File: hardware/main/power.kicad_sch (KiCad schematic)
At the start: 32 parts, among them Q1 SSM3J338R, Q2 BCP53, Q3 SSM3J338R, Q4 BC817, Q5 SSM3J338R, Q6 BC807, Q7 BC817, Q8 BC817, U5 AP2114H-3.3, U7 LM358

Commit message: WIP: Design of PCB
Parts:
- added R21: 0, Resistor_SMD:R_0603_1608Metric_Pad0.98x0.95mm_HandSolder, symbol Device:R
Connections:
- net +BATT: now also R21.1; no longer JP1.1 (A), Q1.3 (D)
- new net: JP1.1 (A), Q1.3 (D), R21.2
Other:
- note added: "TODO: polarity-proof connectors for the batteries"
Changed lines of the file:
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@@
     (stroke (width 0) (type solid) (color 0 0 0 0))
   )
-  (wire (pts (xy 227.33 49.53) (xy 227.33 46.99))
+  (wire (pts (xy 227.33 46.99) (xy 227.33 55.88))
     (stroke (width 0) (type solid) (color 0 0 0 0))
   )
@@
     (stroke (width 0) (type solid) (color 0 0 0 0))
   )
+  (wire (pts (xy 231.14 55.88) (xy 227.33 55.88))
+    (stroke (width 0) (type solid) (color 0 0 0 0))
+  )
   (wire (pts (xy 237.49 31.75) (xy 237.49 29.21))
     (stroke (width 0) (type solid) (color 0 0 0 0))
   )
+  (wire (pts (xy 238.76 55.88) (xy 242.57 55.88))
+    (stroke (width 0) (type solid) (color 0 0 0 0))
+  )
   (wire (pts (xy 242.57 46.99) (xy 240.03 46.99))
     (stroke (width 0) (type solid) (color 0 0 0 0))
   )
-  (wire (pts (xy 242.57 46.99) (xy 242.57 49.53))
-    (stroke (width 0) (type solid) (color 0 0 0 0))
-  )
-  (wire (pts (xy 242.57 49.53) (xy 227.33 49.53))
+  (wire (pts (xy 242.57 46.99) (xy 242.57 55.88))
     (stroke (width 0) (type solid) (color 0 0 0 0))
   )
@@
     (effects (font (size 1.27 1.27)) (justify left bottom))
   )
+  (text "TODO: polarity-proof connectors for the batteries" (at 246.38 129.54 180)
+    (effects (font (size 1.27 1.27)) (justify right bottom))
+  )
   (hierarchical_label "VCC_SW" (shape output) (at 120.65 140.97 90)
     (effects (font (size 1.27 1.27)) (justify left))
@@
       (effects (font (size 1.27 1.27)) hide)
     )
+  )
+  (symbol (lib_id "Device:R") (at 234.95 55.88 90) (unit 1)
+    (in_bom yes) (on_board yes)
+    (property "Reference" "R21" (id 0) (at 234.95 50.6538 90))
+    (property "Value" "0" (id 1) (at 234.95 52.9525 90))
+    (property "Footprint" "Resistor_SMD:R_0603_1608Metric_Pad0.98x0.95mm_HandSolder" (id 2) (at 234.95 57.658 90)
+      (effects (font (size 1.27 1.27)) hide)
+    )
+    (property "Datasheet" "~" (id 3) (at 234.95 55.88 0)
+      (effects (font (size 1.27 1.27)) hide)
+    )

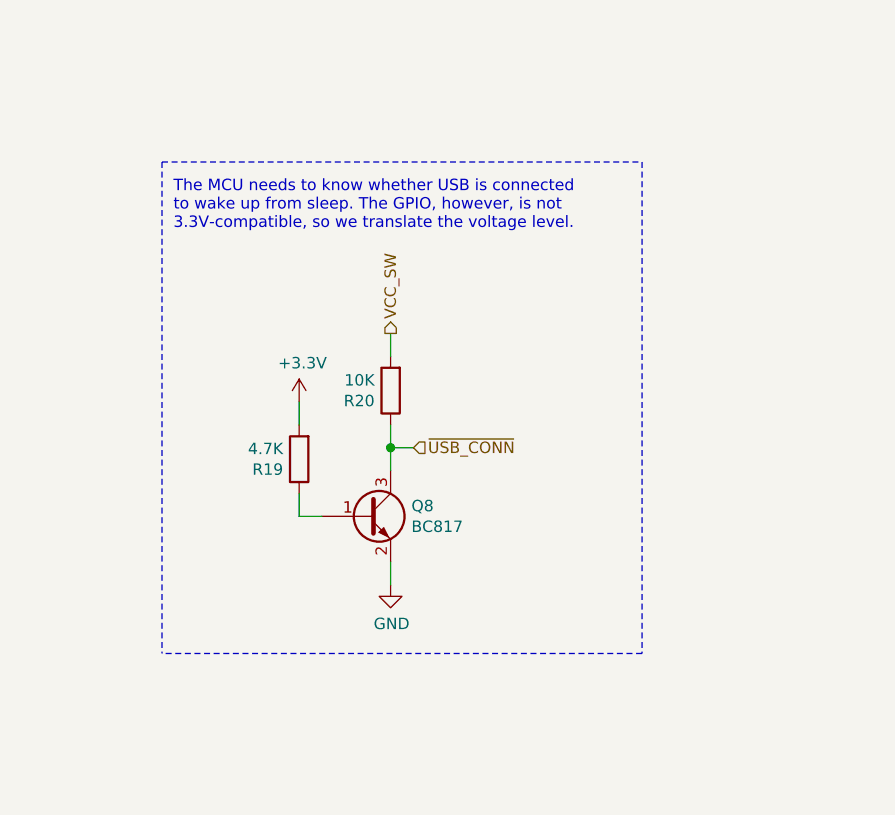
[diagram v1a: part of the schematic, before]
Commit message: Remove the USB sense curcuit
As V_BUS is connected to the MCU it can detect when the USB is
connected.
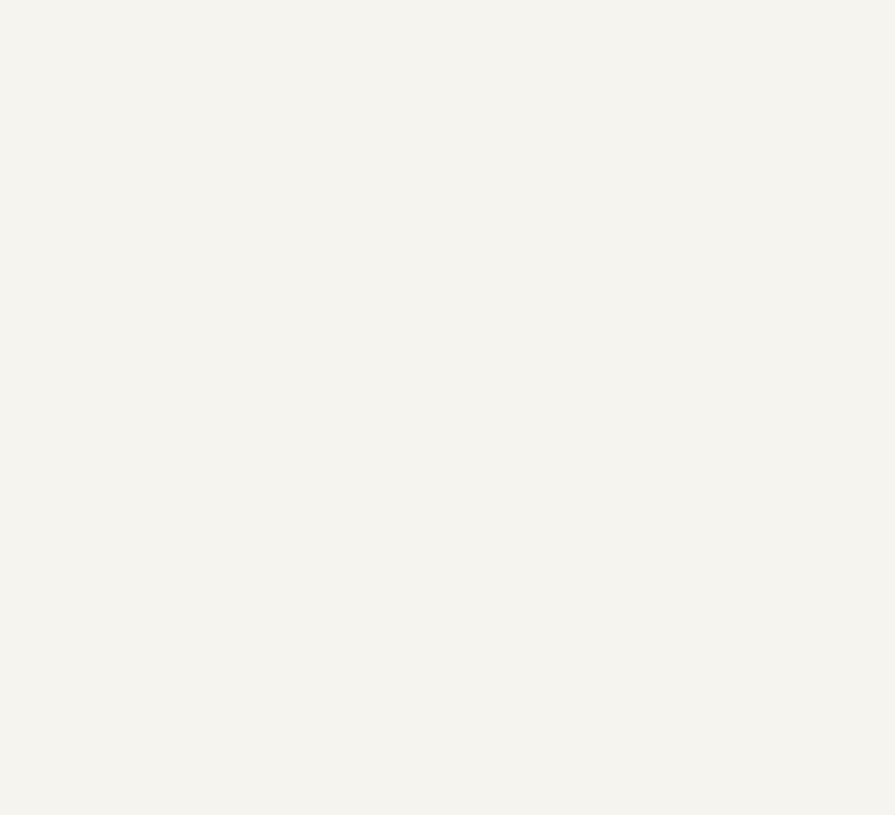
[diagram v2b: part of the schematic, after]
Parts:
- removed Q8: BC817, Package_TO_SOT_SMD:SOT-23, symbol Transistor_BJT:BC817
- removed R19: 4.7K, Resistor_SMD:R_0603_1608Metric, symbol Device:R
- removed R20: 10K, Resistor_SMD:R_0603_1608Metric, symbol Device:R
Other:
- note removed: "The MCU needs to know whether USB is connected to wake up from sleep. The GPIO, however, is not 3.3V-compatible, so we translate the voltage level."
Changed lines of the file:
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@@
   (junction (at 74.93 55.88) (diameter 1.016) (color 0 0 0 0))
   (junction (at 97.79 39.37) (diameter 1.016) (color 0 0 0 0))
-  (junction (at 120.65 153.67) (diameter 1.016) (color 0 0 0 0))
   (junction (at 137.16 39.37) (diameter 1.016) (color 0 0 0 0))
   (junction (at 137.16 52.07) (diameter 1.016) (color 0 0 0 0))
@@
     (stroke (width 0) (type solid) (color 0 0 0 0))
   )
-  (wire (pts (xy 110.49 148.59) (xy 110.49 151.13))
-    (stroke (width 0) (type solid) (color 0 0 0 0))
-  )
-  (wire (pts (xy 110.49 158.75) (xy 110.49 161.29))
-    (stroke (width 0) (type solid) (color 0 0 0 0))
-  )
-  (wire (pts (xy 110.49 161.29) (xy 113.03 161.29))
-    (stroke (width 0) (type solid) (color 0 0 0 0))
-  )
-  (wire (pts (xy 120.65 140.97) (xy 120.65 143.51))
-    (stroke (width 0) (type solid) (color 0 0 0 0))
-  )
-  (wire (pts (xy 120.65 151.13) (xy 120.65 153.67))
-    (stroke (width 0) (type solid) (color 0 0 0 0))
-  )
-  (wire (pts (xy 120.65 153.67) (xy 120.65 156.21))
-    (stroke (width 0) (type solid) (color 0 0 0 0))
-  )
-  (wire (pts (xy 120.65 153.67) (xy 123.19 153.67))
-    (stroke (width 0) (type solid) (color 0 0 0 0))
-  )
-  (wire (pts (xy 120.65 166.37) (xy 120.65 168.91))
-    (stroke (width 0) (type solid) (color 0 0 0 0))
-  )
   (wire (pts (xy 127 69.85) (xy 127 72.39))
     (stroke (width 0) (type solid) (color 0 0 0 0))
@@
     (stroke (width 0) (type dash) (color 0 0 0 0))
   )
-  (polyline (pts (xy 95.25 121.92) (xy 95.25 176.53))
-    (stroke (width 0) (type dash) (color 0 0 0 0))
-  )
-  (polyline (pts (xy 95.25 121.92) (xy 148.59 121.92))
-    (stroke (width 0) (type dash) (color 0 0 0 0))
-  )
   (polyline (pts (xy 113.03 17.78) (xy 113.03 100.33))
     (stroke (width 0) (type dash) (color 0 0 0 0))
@@
   )
   (polyline (pts (xy 115.57 17.78) (xy 161.29 17.78))
-    (stroke (width 0) (type dash) (color 0 0 0 0))
-  )
-  (polyline (pts (xy 148.59 121.92) (xy 148.59 176.53))
-    (stroke (width 0) (type dash) (color 0 0 0 0))
-  )
-  (polyline (pts (xy 148.59 176.53) (xy 95.25 176.53))
     (stroke (width 0) (type dash) (color 0 0 0 0))
   )
@@
     (effects (font (size 1.27 1.27)) (justify left bottom))
   )
-  (text "The MCU needs to know whether USB is connected\nto wake up from sleep. The GPIO, however, is not\n3.3V-compatible, so we translate the voltage level."
-    (at 96.52 129.54 0)
-    (effects (font (size 1.27 1.27)) (justify left bottom))
-  )
   (text "A bidirectional switch is required to prevent\ncurrent flowing through the constant curren\nsource during battery operation."
     (at 116.84 25.4 0)
@@
     (effects (font (size 1.27 1.27)) (justify right bottom))
   )
-  (hierarchical_label "VCC_SW" (shape output) (at 120.65 140.97 90)
-    (effects (font (size 1.27 1.27)) (justify left))
-  )
-  (hierarchical_label "~USB_CONN" (shape input) (at 123.19 153.67 0)
-    (effects (font (size 1.27 1.27)) (justify left))
-  )
   (hierarchical_label "CHARGE" (shape input) (at 127 69.85 90)
     (effects (font (size 1.27 1.27)) (justify left))
@@
     )
   )
-  (symbol (lib_id "power:+3.3V") (at 110.49 148.59 0) (unit 1)
-    (in_bom yes) (on_board yes)
-    (property "Reference" "#PWR0140" (id 0) (at 110.49 152.4 0)
-      (effects (font (size 1.27 1.27)) hide)
-    )
-    (property "Value" "+3.3V" (id 1) (at 110.8583 144.2656 0))
-    (property "Footprint" "" (id 2) (at 110.49 148.59 0)
-      (effects (font (size 1.27 1.27)) hide)
-    )
-    (property "Datasheet" "" (id 3) (at 110.49 148.59 0)
-      (effects (font (size 1.27 1.27)) hide)
-    )
-  )
   (symbol (lib_id "power:+BATT") (at 210.82 36.83 0) (unit 1)
     (in_bom yes) (on_board yes)
@@
     )
   )
-  (symbol (lib_id "power:GND") (at 120.65 168.91 0) (unit 1)
-    (in_bom yes) (on_board yes)
-    (property "Reference" "#PWR0141" (id 0) (at 120.65 175.26 0)
-      (effects (font (size 1.27 1.27)) hide)
-    )
-    (property "Value" "GND" (id 1) (at 120.7643 173.2344 0))
-    (property "Footprint" "" (id 2) (at 120.65 168.91 0)
-      (effects (font (size 1.27 1.27)) hide)
-    )
-    (property "Datasheet" "" (id 3) (at 120.65 168.91 0)
-      (effects (font (size 1.27 1.27)) hide)
-    )
-  )
   (symbol (lib_id "power:GND") (at 210.82 92.71 0) (unit 1)
     (in_bom yes) (on_board yes)
@@
     )
     (property "Mouser" "588-KDV12FR510ET" (id 5) (at 91.44 39.37 0)
-      (effects (font (size 1.27 1.27)) hide)
-    )
-  )
-  (symbol (lib_id "Device:R") (at 110.49 154.94 180) (unit 1)
-    (in_bom yes) (on_board yes)
-    (property "Reference" "R19" (id 0) (at 108.7119 156.0894 0)
-      (effects (font (size 1.27 1.27)) (justify left))
-    )
-    (property "Value" "4.7K" (id 1) (at 108.712 153.791 0)
-      (effects (font (size 1.27 1.27)) (justify left))
-    )
-    (property "Footprint" "Resistor_SMD:R_0603_1608Metric" (id 2) (at 112.268 154.94 90)
-      (effects (font (size 1.27 1.27)) hide)
-    )
-    (property "Datasheet" "~" (id 3) (at 110.49 154.94 0)
-      (effects (font (size 1.27 1.27)) hide)
-    )
-  )
-  (symbol (lib_id "Device:R") (at 120.65 147.32 180) (unit 1)
-    (in_bom yes) (on_board yes)
-    (property "Reference" "R20" (id 0) (at 118.8719 148.4694 0)
-      (effects (font (size 1.27 1.27)) (justify left))
-    )
-    (property "Value" "10K" (id 1) (at 118.872 146.171 0)
-      (effects (font (size 1.27 1.27)) (justify left))
-    )
-    (property "Footprint" "Resistor_SMD:R_0603_1608Metric" (id 2) (at 122.428 147.32 90)
-      (effects (font (size 1.27 1.27)) hide)
-    )
-    (property "Datasheet" "~" (id 3) (at 120.65 147.32 0)
       (effects (font (size 1.27 1.27)) hide)
     )
@@
     )
   )
-  (symbol (lib_id "Transistor_BJT:BC817") (at 118.11 161.29 0) (unit 1)
-    (in_bom yes) (on_board yes)
-    (property "Reference" "Q8" (id 0) (at 122.9615 160.1406 0)
-      (effects (font (size 1.27 1.27)) (justify left))
-    )
-    (property "Value" "BC817" (id 1) (at 122.9615 162.4393 0)
-      (effects (font (size 1.27 1.27)) (justify left))
-    )
-    (property "Footprint" "Package_TO_SOT_SMD:SOT-23" (id 2) (at 123.19 163.195 0)
-      (effects (font (size 1.27 1.27) italic) (justify left) hide)
-    )
-    (property "Datasheet" "https://www.onsemi.com/pub/Collateral/BC818-D.pdf" (id 3) (at 118.11 161.29 0)
-      (effects (font (size 1.27 1.27)) (justify left) hide)
-    )
-  )
